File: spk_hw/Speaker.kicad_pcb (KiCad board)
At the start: 2 copper layers, 45 x 22.5 mm, 42 parts, among them J1 Conn_01x04, SW1 SW_Push, U1 CH591F, U2 MAX98357A, U3 TPS61099DRV, U4 XS3A1T3157, U5 XC6206P332, U6 MT3608L, Y1 32MHz

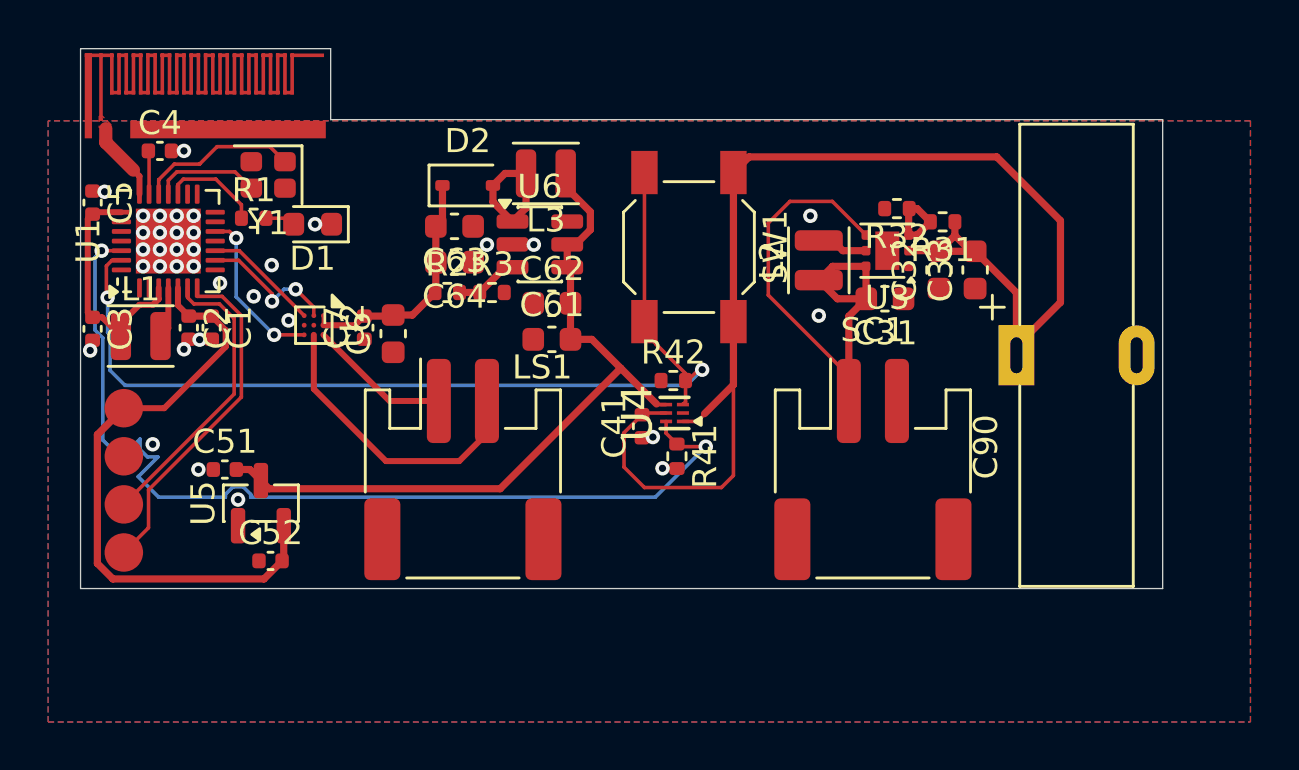
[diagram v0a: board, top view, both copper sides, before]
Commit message: spk_hw: Add many vias
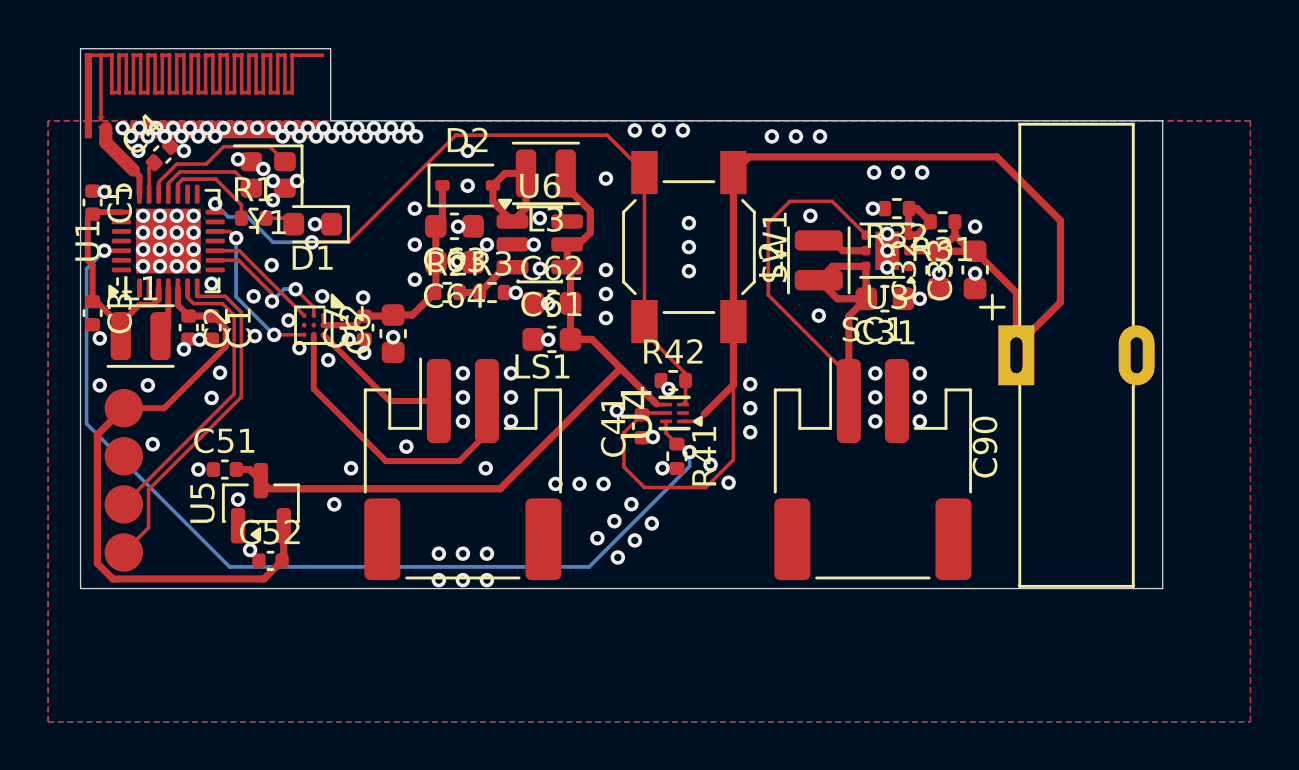
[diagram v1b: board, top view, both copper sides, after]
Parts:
- moved C3 0.65 mm to (121.8, 63.0)
- moved C4 0.18 mm to (124.8, 56.4), turned to 45 degrees
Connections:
- U1 pad 14: unconnected-(U1-PB7/TXD0/PWM9-Pad14) -> /BTN
- U1 pad 27: /BTN -> unconnected-(U1-PA13/SCK0/PWM5/AIN3-Pad27)
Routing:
- net /BTN: track 41.6 -> 31.7 mm
- net /PWR_LATCH: track 41.3 -> 39.9 mm
- net GND: vias 35 -> 161
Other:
- board text added: "CPW W = 0.55 mm, S = 0.12 mm H = 1.4 mm, T = 0.035 mm (1.6 mm / 1 oz) Z_{0} = 51.385 Ω"

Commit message: spk_hw: Sign off
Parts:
- added G***: LOGO, LOGO, B.Cu at (158.3, 71.9)
- added G***: LOGO, LOGO, B.Cu at (163.5, 71.7)
- moved D1 0.05 mm to (131.0, 59.4)
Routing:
- net GND: vias 161 -> 165
- added copper zone on F.Cu, net Net-(D2-A)
- added copper zone on F.Cu, net Net-(SC1-+)
- added copper zone on F.Cu, net Net-(U3-FB)
- added copper zone on F.Cu, net VBAT
- added copper zone on F.Cu, net VBAT_ON
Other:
- outline, holes or cut-outs redrawn
- board text added: "+"
- board text added: "<26-"
- board text added: ">"
- board text added: "Rev. 1"
- board text added: "春分"

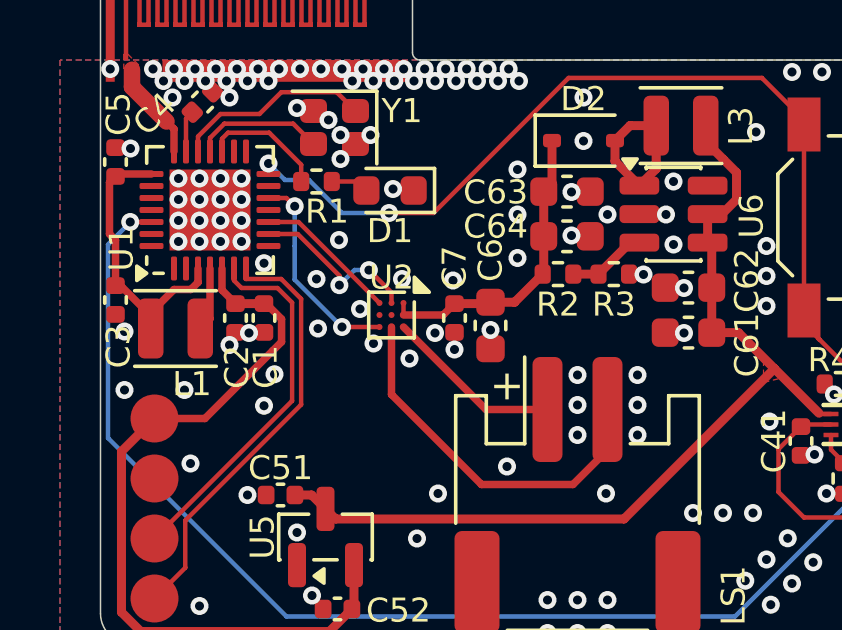
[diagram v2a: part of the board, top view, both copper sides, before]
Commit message: spk_hw: Increase BGA pad size due to fabricator constraints >_<
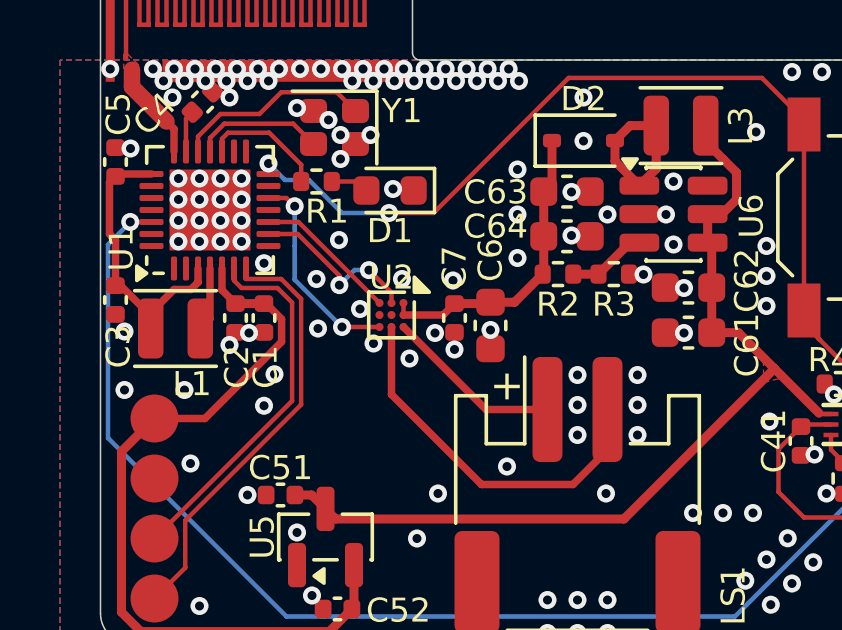
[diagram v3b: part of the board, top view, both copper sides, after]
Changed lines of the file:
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@@
+			)
+		)
+		(property "LCSC PN" "C318884"
+			(at 0 0 270)
+			(unlocked yes)
+			(layer "F.Fab")
+			(hide yes)
+			(effects
+				(font
+					(size 1 1)
+					(thickness 0.15)
+				)
 			)
 		)
@@
 		(pad "A1" smd circle
 			(at -0.4 -0.4 270)
-			(size 0.2 0.2)
+			(size 0.27 0.27)
 			(property pad_prop_bga)
 			(layers "F.Cu" "F.Mask" "F.Paste")
@@
 		(pad "A2" smd circle
 			(at 0 -0.4 270)
-			(size 0.2 0.2)
+			(size 0.27 0.27)
 			(property pad_prop_bga)
 			(layers "F.Cu" "F.Mask" "F.Paste")
@@
 		(pad "A3" smd circle
 			(at 0.4 -0.4 270)
-			(size 0.2 0.2)
+			(size 0.27 0.27)
 			(property pad_prop_bga)
 			(layers "F.Cu" "F.Mask" "F.Paste")
@@
 		(pad "B1" smd circle
 			(at -0.4 0 270)
-			(size 0.2 0.2)
+			(size 0.27 0.27)
 			(property pad_prop_bga)
 			(layers "F.Cu" "F.Mask" "F.Paste")
@@
 		(pad "B2" smd circle
 			(at 0 0 270)
-			(size 0.2 0.2)
+			(size 0.27 0.27)
 			(property pad_prop_bga)
 			(layers "F.Cu" "F.Mask" "F.Paste")
@@
 		(pad "B3" smd circle
 			(at 0.4 0 270)
-			(size 0.2 0.2)
+			(size 0.27 0.27)
 			(property pad_prop_bga)
 			(layers "F.Cu" "F.Mask" "F.Paste")
@@
 		(pad "C1" smd circle
 			(at -0.4 0.4 270)
-			(size 0.2 0.2)
+			(size 0.27 0.27)
 			(property pad_prop_bga)
 			(layers "F.Cu" "F.Mask" "F.Paste")
@@
 		(pad "C2" smd circle
 			(at 0 0.4 270)
-			(size 0.2 0.2)
+			(size 0.27 0.27)
 			(property pad_prop_bga)
 			(layers "F.Cu" "F.Mask" "F.Paste")
@@
 		(pad "C3" smd circle
 			(at 0.4 0.4 270)
-			(size 0.2 0.2)
+			(size 0.27 0.27)
 			(property pad_prop_bga)
 			(layers "F.Cu" "F.Mask" "F.Paste")
